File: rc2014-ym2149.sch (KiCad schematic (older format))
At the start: 23 parts, among them J1 JACK_TRS_6PINS, P1 CONN_01X35, P2 CONN_02X08, P3 AY-3-8190/YM2149F, P4 IO Out, U1 74HCT138, U3 74HCT00, U4 74HCT74

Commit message: Messing about with address decoding
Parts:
- added J? (x2): CONN_02X08, symbol CONN_02X08
- added J?: CONN_02X03, symbol CONN_02X03
- added U? (x2): 74HCT00, symbol 74HCT00
- added U?: 74LS138, symbol 74LS138
- P2: value CONN_02X08 -> CONN_02X09; symbol CONN_02X08 -> CONN_02X09
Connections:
- net labels added: /AY_CS, /E2, E3, REG
- wire segments 166 -> 248
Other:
- moved on the sheet: U1, U3A, U3B

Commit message: More work on PCB
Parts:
- removed J?: CONN_02X08, symbol CONN_02X08
- removed P2: CONN_02X09, Pin_Headers:Pin_Header_Straight_2x08_Pitch2.54mm, symbol CONN_02X09
- removed U? (x2): 74HCT00, symbol 74HCT00
- removed U?: 74LS138, symbol 74LS138
- added C7: C, Capacitors_THT:C_Disc_D3.8mm_W2.6mm_P2.50mm, symbol C
- added J2, J3: CONN_02X02, Pin_Headers:Pin_Header_Straight_2x02_Pitch2.54mm, symbol CONN_02X02
- added U2: 74HCT138, Housings_DIP:DIP-16_W7.62mm_Socket, symbol 74LS138
- added unit 3 of U3
- added unit 4 of U3
- J4: renamed from J?; footprint (none) -> Pin_Headers:Pin_Header_Straight_2x03_Pitch2.54mm
- J5: renamed from J?; footprint (none) -> Pin_Headers:Pin_Header_Straight_2x08_Pitch2.54mm
- P1: value CONN_01X35 -> RC2014 BUS; footprint Pin_Headers:Pin_Header_Angled_1x35_Pitch2.54mm -> Pin_Headers:Pin_Header_Angled_1x39_Pitch2.54mm; symbol CONN_01X35 -> CONN_01X39
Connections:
- net labels added: CS
- net labels removed: /AY_CS, /E2, E3
- wire segments 248 -> 210
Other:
- moved on the sheet: C4, C6, J5

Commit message: WIP
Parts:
- J1: value JACK_TRS_6PINS -> AUDIO OUT
- JP1: renamed from J2; value CONN_02X02 -> USE A4 FOR ENABLE; symbol CONN_02X02 -> Jumper_Dual
- JP2: renamed from J3; value CONN_02X02 -> ENABLE SELECTOR; symbol CONN_02X02 -> Jumper_Dual
- JP4: renamed from J5; value CONN_02X08 -> BASE ADDRESS
- JP5: renamed from JP1; value Jumper_Dual -> CLOCK DIVIDE 1/2 or 1/4
- renumbered C4 to C1, C5 to C2, C6 to C3, C7 to C4, C1 to C5, C2 to C6, C3 to C7, P4 to J2, J4 to JP3, JP3 to JP6, U2 to U1, U1 to U2, P3 to U5
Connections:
- wire segments 210 -> 207
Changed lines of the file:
@@
 $EndComp
 $Comp
-L DIL40 P3
+L DIL40 U5
 U 1 1 58979138
 P 6600 3100
-F 0 "P3" H 6600 4150 50  0000 C CNN
+F 0 "U5" H 6600 4150 50  0000 C CNN
 F 1 "AY-3-8190/YM2149F" V 6600 3100 50  0000 C CNN
 F 2 "Housings_DIP:DIP-40_W15.24mm_Socket" H 6600 3100 50  0001 C CNN
@@
 $EndComp
 $Comp
-L 74LS138 U1
+L 74LS138 U2
 U 1 1 589793B1
 P 3450 3200
-F 0 "U1" H 3550 3700 50  0000 C CNN
+F 0 "U2" H 3550 3700 50  0000 C CNN
 F 1 "74HCT138" H 3600 2651 50  0000 C CNN
 F 2 "Housings_DIP:DIP-16_W7.62mm_Socket" H 3450 3200 50  0001 C CNN
@@
 P 10150 1000
 F 0 "J1" H 10150 1400 50  0000 C CNN
-F 1 "JACK_TRS_6PINS" H 10100 700 50  0000 C CNN
+F 1 "AUDIO OUT" H 10100 700 50  0000 C CNN
 F 2 "rc2014:cliff_fcr1295_socket" H 10250 850 50  0001 C CNN
 F 3 "" H 10250 850 50  0000 C CNN
@@
 $EndComp
 $Comp
-L C C1
+L C C5
 U 1 1 58B2B931
 P 7200 2000
-F 0 "C1" H 7225 2100 50  0000 L CNN
+F 0 "C5" H 7225 2100 50  0000 L CNN
 F 1 "0.1uF" H 7225 1900 50  0000 L CNN
 F 2 "Capacitors_THT:C_Disc_D3.8mm_W2.6mm_P2.50mm" H 7238 1850 50  0001 C CNN
@@
 	1    0    0    -1
 $EndComp
-Text Label 2700 2950 0    60   ~ 0
+Text Label 2650 2950 0    60   ~ 0
 /WR
-Text Label 2700 3050 0    60   ~ 0
+Text Label 2650 3050 0    60   ~ 0
 /RD
-Text Label 2700 3550 0    60   ~ 0
+Text Label 2650 3550 0    60   ~ 0
 /IORQ
 $Comp
-L Jumper JP3
+L Jumper JP6
 U 1 1 58BC56E2
 P 8650 3550
-F 0 "JP3" H 8650 3700 50  0000 C CNN
+F 0 "JP6" H 8650 3700 50  0000 C CNN
 F 1 "YM 1/2 CLK" H 8650 3470 50  0000 C CNN
 F 2 "Pin_Headers:Pin_Header_Straight_1x02_Pitch2.54mm" H 8650 3550 50  0001 C CNN
@@
 	6000 4150 6100 4050
 $Comp
-L CONN_02X09 P4
+L CONN_02X09 J2
 U 1 1 58BC7A79
 P 10450 2700
-F 0 "P4" H 10450 3200 50  0000 C CNN
+F 0 "J2" H 10450 3200 50  0000 C CNN
 F 1 "IO Out" V 10450 2700 50  0000 C CNN
 F 2 "Pin_Headers:Pin_Header_Straight_2x09_Pitch2.54mm" H 10450 1500 50  0001 C CNN
@@
 	7350 4100 7450 4200
 $Comp
-L CP C2
+L CP C6
 U 1 1 58BDC9B3
 P 9000 800
-F 0 "C2" H 9025 900 50  0000 L CNN
+F 0 "C6" H 9025 900 50  0000 L CNN
 F 1 "470uF" H 9025 700 50  0000 L CNN
 F 2 "Capacitors_THT:CP_Radial_D5.0mm_P2.50mm" H 9038 650 50  0001 C CNN
@@
 $EndComp
 $Comp
-L CP C3
+L CP C7
 U 1 1 58BDCA34
 P 9000 1000
-F 0 "C3" H 9025 1100 50  0000 L CNN
+F 0 "C7" H 9025 1100 50  0000 L CNN
 F 1 "470uF" H 9025 900 50  0000 L CNN
 F 2 "Capacitors_THT:CP_Radial_D5.0mm_P2.50mm" H 9038 850 50  0001 C CNN
@@
 D7
 $Comp
-L C C4
+L C C1
 U 1 1 58C9A12D
 P 2550 6400
-F 0 "C4" H 2575 6500 50  0000 L CNN
+F 0 "C1" H 2575 6500 50  0000 L CNN
 F 1 "C" H 2575 6300 50  0000 L CNN
 F 2 "Capacitors_THT:C_Disc_D3.8mm_W2.6mm_P2.50mm" H 2588 6250 50  0001 C CNN
@@
 $EndComp
 $Comp
-L C C5
+L C C2
 U 1 1 58C9A196
 P 2900 6400
-F 0 "C5" H 2925 6500 50  0000 L CNN
+F 0 "C2" H 2925 6500 50  0000 L CNN
 F 1 "C" H 2925 6300 50  0000 L CNN
 F 2 "Capacitors_THT:C_Disc_D3.8mm_W2.6mm_P2.50mm" H 2938 6250 50  0001 C CNN
@@
 $EndComp
 $Comp
-L C C6
+L C C3
 U 1 1 58C9A1DD
 P 3250 6400
-F 0 "C6" H 3275 6500 50  0000 L CNN
+F 0 "C3" H 3275 6500 50  0000 L CNN
 F 1 "C" H 3275 6300 50  0000 L CNN
 F 2 "Capacitors_THT:C_Disc_D3.8mm_W2.6mm_P2.50mm" H 3288 6250 50  0001 C CNN
@@
 BC1
 $Comp
-L Jumper_Dual JP1
+L Jumper_Dual JP5
 U 1 1 58D043AC
 P 7450 5350
-F 0 "JP1" H 7500 5250 50  0000 L CNN
-F 1 "Jumper_Dual" H 7450 5450 50  0000 C BNN
+F 0 "JP5" H 7500 5250 50  0000 L CNN
+F 1 "CLOCK DIVIDE 1/2 or 1/4" H 7450 5450 50  0000 C BNN
 F 2 "Pin_Headers:Pin_Header_Straight_1x03_Pitch2.54mm" H 7450 5350 50  0001 C CNN
 F 3 "" H 7450 5350 50  0001 C CNN
@@
 Text Label 2700 2850 0    60   ~ 0
 REG
-Text Label 2750 3450 0    60   ~ 0
+Text Label 2650 3450 0    60   ~ 0
 A1
 Wire Wire Line
@@
 	1100 4100 1350 4100
 Wire Wire Line
-	2900 2950 2700 2950
-Wire Wire Line
-	2900 3050 2700 3050
-Wire Wire Line
-	2900 3550 2700 3550
+	2850 2950 2650 2950
+Wire Wire Line
+	2850 3050 2650 3050
 Connection ~ 7200 2150
 Wire Wire Line
@@
 	7700 5100 7700 5350
 Wire Wire Line
-	2500 3350 2850 3350
-Wire Wire Line
-	2850 3450 2700 3450
+	2250 3350 2850 3350
 Wire Wire Line
 	1100 1800 1350 1800
@@
 Wire Wire Line
 	2600 2850 2850 2850
-Text Label 1850 3350 0    60   ~ 0
+Text Label 1800 3200 0    60   ~ 0
 A15
 $Comp
-L CONN_02X03 J4
+L CONN_02X03 JP3
 U 1 1 58DAC18B
 P 2300 2700
-F 0 "J4" H 2300 2900 50  0000 C CNN
+F 0 "JP3" H 2300 2900 50  0000 C CNN
 F 1 "CONN_02X03" H 2300 2500 50  0000 C CNN
 F 2 "Pin_Headers:Pin_Header_Straight_2x03_Pitch2.54mm" H 2300 1500 50  0001 C CNN
@@
 Wire Wire Line
 	2050 2800 1850 2800
-Text Label 1900 2700 0    60   ~ 0
+Text Label 1850 2700 0    60   ~ 0
 A3
-Text Label 1900 2800 0    60   ~ 0
+Text Label 1850 2800 0    60   ~ 0
 A2
-Text Label 1900 2600 0    60   ~ 0
+Text Label 1850 2600 0    60   ~ 0
 A14
 $Comp
-L CONN_02X08 J5
+L CONN_02X08 JP4
 U 1 1 58DAD194
 P 3550 1150
-F 0 "J5" H 3550 1600 50  0000 C CNN
-F 1 "CONN_02X08" V 3550 1150 50  0000 C CNN
+F 0 "JP4" H 3550 1600 50  0000 C CNN
+F 1 "BASE ADDRESS" V 3550 1150 50  0000 C CNN
 F 2 "Pin_Headers:Pin_Header_Straight_2x08_Pitch2.54mm" H 3550 -50 50  0001 C CNN
 F 3 "" H 3550 -50 50  0001 C CNN
@@
 Connection ~ 3950 1500
 $Comp
-L 74LS138 U2
+L 74LS138 U1
 U 1 1 58DAFD76
 P 2550 1150
-F 0 "U2" H 2650 1650 50  0000 C CNN
+F 0 "U1" H 2650 1650 50  0000 C CNN
 F 1 "74HCT138" H 2700 601 50  0000 C CNN
 F 2 "Housings_DIP:DIP-16_W7.62mm_Socket" H 2550 1150 50  0001 C CNN
@@
 Wire Wire Line
 	1950 1000 1700 1000
-Wire Wire Line
-	1550 1300 1950 1300
 Wire Wire Line
 	1950 1400 1700 1400
@@
 A7
 $Comp
-L CONN_02X02 J2
+L Jumper_Dual JP1
 U 1 1 58DB01E6
-P 1300 1250
-F 0 "J2" H 1300 1400 50  0000 C CNN
-F 1 "CONN_02X02" H 1300 1100 50  0000 C CNN
-F 2 "Pin_Headers:Pin_Header_Straight_2x02_Pitch2.54mm" H 1300 50  50  0001 C CNN
-F 3 "" H 1300 50  50  0001 C CNN
-	1    1300 1250
-	1    0    0    -1
-$EndComp
-Wire Wire Line
-	1550 1200 1600 1200
-Wire Wire Line
-	1600 1200 1600 1300
-Connection ~ 1600 1300
+P 1100 1100
+F 0 "JP1" H 1100 1250 50  0000 C CNN
+F 1 "USE A4 FOR ENABLE" H 1150 800 50  0000 C CNN
+F 2 "Pin_Headers:Pin_Header_Straight_2x02_Pitch2.54mm" H 1100 -100 50  0001 C CNN
+F 3 "" H 1100 -100 50  0001 C CNN
+	1    1100 1100
+	1    0    0    -1
+$EndComp
 Wire Wire Line
 	1700 1400 1700 1600
@@
 	1    0    0    -1
 $EndComp
-Wire Wire Line
-	1050 1200 850  1200
-Wire Wire Line
-	1050 1300 850  1300
-Text Label 900  1300 0    60   ~ 0
+Text Label 1400 1100 0    60   ~ 0
 A4
 $Comp
 L VCC #PWR024
 U 1 1 58DB09C6
-P 850 1200
-F 0 "#PWR024" H 850 1050 50  0001 C CNN
-F 1 "VCC" H 850 1350 50  0000 C CNN
-F 2 "" H 850 1200 50  0001 C CNN
-F 3 "" H 850 1200 50  0001 C CNN
-	1    850  1200
-	1    0    0    -1
+P 850 1100
+F 0 "#PWR024" H 850 950 50  0001 C CNN
+F 1 "VCC" H 850 1250 50  0000 C CNN
+F 2 "" H 850 1100 50  0001 C CNN
+F 3 "" H 850 1100 50  0001 C CNN
+	1    850  1100
+	0    -1   -1   0
 $EndComp
 Connection ~ 1700 1500
@@
 CS
 $Comp
-L CONN_02X02 J3
+L Jumper_Dual JP2
 U 1 1 58DB0BB0
-P 2250 3400
-F 0 "J3" H 2250 3550 50  0000 C CNN
-F 1 "CONN_02X02" H 2250 3250 50  0000 C CNN
-F 2 "Pin_Headers:Pin_Header_Straight_2x02_Pitch2.54mm" H 2250 2200 50  0001 C CNN
-F 3 "" H 2250 2200 50  0001 C CNN
-	1    2250 3400
-	1    0    0    -1
-$EndComp
-Wire Wire Line
-	2000 3350 1850 3350
-Wire Wire Line
-	2000 3450 1850 3450
-Wire Wire Line
-	2500 3450 2550 3450
-Wire Wire Line
-	2550 3450 2550 3350
-Connection ~ 2550 3350
-Text Label 1850 3450 0    60   ~ 0
+P 2250 3200
+F 0 "JP2" H 2250 3350 50  0000 C CNN
+F 1 "ENABLE SELECTOR" H 2250 2850 50  0000 C CNN
+F 2 "Pin_Headers:Pin_Header_Straight_2x02_Pitch2.54mm" H 2250 2000 50  0001 C CNN
+F 3 "" H 2250 2000 50  0001 C CNN
+	1    2250 3200
+	1    0    0    -1
+$EndComp
+Text Label 2550 3200 0    60   ~ 0
 CS
 $Comp
@@
 $EndComp
 $Comp
-L C C7
+L C C4
 U 1 1 58DB1AE2
 P 3600 6400
-F 0 "C7" H 3625 6500 50  0000 L CNN
+F 0 "C4" H 3625 6500 50  0000 L CNN
 F 1 "C" H 3625 6300 50  0000 L CNN
 F 2 "Capacitors_THT:C_Disc_D3.8mm_W2.6mm_P2.50mm" H 3638 6250 50  0001 C CNN
@@
 	1    0    0    -1
 $EndComp
+Wire Wire Line
+	2850 3450 2650 3450
+Wire Wire Line
+	2850 3550 2650 3550
+Wire Wire Line
+	1350 1100 1550 1100
+Wire Wire Line
+	1100 1300 1950 1300
+Wire Wire Line
+	1100 1300 1100 1200
+Wire Wire Line
+	2000 3200 1800 3200
+Wire Wire Line
+	2500 3200 2750 3200
+Wire Wire Line
+	2250 3350 2250 3300
 $EndSCHEMATC

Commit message: Fix all ERC errors
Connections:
- no-connect marks 0 -> 25
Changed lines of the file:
@@
 	1100 3400 1650 3400
 Wire Wire Line
-	1100 3500 1350 3500
+	1100 3500 1450 3500
 Wire Wire Line
 	1100 3700 1350 3700
@@
 Wire Wire Line
 	2250 3350 2250 3300
+$Comp
+L PWR_FLAG #FLG028
+U 1 1 58E0E873
+P 1550 3400
+F 0 "#FLG028" H 1550 3475 50  0001 C CNN
+F 1 "PWR_FLAG" H 1550 3550 50  0000 C CNN
+F 2 "" H 1550 3400 50  0001 C CNN
+F 3 "" H 1550 3400 50  0001 C CNN
+	1    1550 3400
+	1    0    0    -1
+$EndComp
+Connection ~ 1550 3400
+$Comp
+L PWR_FLAG #FLG029
+U 1 1 58E0EDBF
+P 1450 3500
+F 0 "#FLG029" H 1450 3575 50  0001 C CNN
+F 1 "PWR_FLAG" H 1450 3650 50  0000 C CNN
+F 2 "" H 1450 3500 50  0001 C CNN
+F 3 "" H 1450 3500 50  0001 C CNN
+	1    1450 3500
+	1    0    0    -1
+$EndComp
+Connection ~ 1350 3500
+NoConn ~ 1100 5200
+NoConn ~ 1100 5300
+NoConn ~ 1100 5400
+NoConn ~ 1100 5500
+NoConn ~ 1100 5600
+NoConn ~ 1350 3900
+NoConn ~ 1350 4000
+NoConn ~ 1350 3600
+NoConn ~ 1350 3300
+NoConn ~ 1350 2500
+NoConn ~ 1350 2400
+NoConn ~ 1350 2300
+NoConn ~ 1350 2200
+NoConn ~ 1350 2100
+NoConn ~ 1350 2000
+NoConn ~ 6250 2250
+NoConn ~ 6250 2550
+NoConn ~ 6950 2250
+NoConn ~ 4050 2850
+NoConn ~ 4050 2950
+NoConn ~ 4050 3050
+NoConn ~ 4050 3450
+NoConn ~ 4050 3550
+NoConn ~ 5650 1150
+NoConn ~ 5650 1850
 $EndSCHEMATC

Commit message: Add ground fill and create gerbers
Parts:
- JP1, JP2: footprint Pin_Headers:Pin_Header_Straight_2x02_Pitch2.54mm -> Pin_Headers:Pin_Header_Straight_1x03_Pitch2.54mm
- P1: footprint Pin_Headers:Pin_Header_Angled_1x39_Pitch2.54mm -> rc2014:Pin_Header_Straight_1x39_Pitch2.54mm_NoSilk
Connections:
- wire segments 207 -> 209
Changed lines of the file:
@@
 F 0 "P1" H 900 5750 50  0000 C CNN
 F 1 "RC2014 BUS" V 1000 3700 50  0000 C CNN
-F 2 "Pin_Headers:Pin_Header_Angled_1x39_Pitch2.54mm" H 900 3700 50  0001 C CNN
+F 2 "rc2014:Pin_Header_Straight_1x39_Pitch2.54mm_NoSilk" H 900 3700 50  0001 C CNN
 F 3 "" H 900 3700 50  0000 C CNN
 	1    900  3700
-	-1   0    0    1
+	-1   0    0    -1
 $EndComp
 $Comp
@@
 	4850 5100 5100 5100
 Wire Wire Line
-	8050 3950 8050 5650
-Wire Wire Line
 	4600 5300 5100 5300
 Wire Wire Line
@@
 Wire Wire Line
 	6300 6650 6900 6650
-Wire Wire Line
-	6300 5100 7700 5100
-Wire Wire Line
-	6900 6650 6900 5350
 Wire Bus Line
 	6000 2750 6000 4200
@@
 Connection ~ 9600 800
 Wire Wire Line
-	8050 5650 7450 5650
-Wire Wire Line
 	7450 5650 7450 5450
 Wire Wire Line
-	6900 5350 7200 5350
-Wire Wire Line
-	7700 5100 7700 5350
-Wire Wire Line
 	2250 3350 2850 3350
 Wire Wire Line
@@
 Wire Wire Line
 	2600 2850 2850 2850
-Text Label 1800 3200 0    60   ~ 0
+Text Label 2600 3200 0    60   ~ 0
 A15
 $Comp
@@
 F 0 "JP1" H 1100 1250 50  0000 C CNN
 F 1 "USE A4 FOR ENABLE" H 1150 800 50  0000 C CNN
-F 2 "Pin_Headers:Pin_Header_Straight_2x02_Pitch2.54mm" H 1100 -100 50  0001 C CNN
+F 2 "Pin_Headers:Pin_Header_Straight_1x03_Pitch2.54mm" H 1100 -100 50  0001 C CNN
 F 3 "" H 1100 -100 50  0001 C CNN
 	1    1100 1100
@@
 F 0 "JP2" H 2250 3350 50  0000 C CNN
 F 1 "ENABLE SELECTOR" H 2250 2850 50  0000 C CNN
-F 2 "Pin_Headers:Pin_Header_Straight_2x02_Pitch2.54mm" H 2250 2000 50  0001 C CNN
+F 2 "Pin_Headers:Pin_Header_Straight_1x03_Pitch2.54mm" H 2250 2000 50  0001 C CNN
 F 3 "" H 2250 2000 50  0001 C CNN
 	1    2250 3200
 	1    0    0    -1
 $EndComp
-Text Label 2550 3200 0    60   ~ 0
+Text Label 1800 3200 0    60   ~ 0
 CS
 $Comp
@@
 NoConn ~ 5650 1150
 NoConn ~ 5650 1850
+Wire Wire Line
+	8050 5650 7450 5650
+Wire Wire Line
+	8050 3950 8050 5650
+Wire Wire Line
+	6900 6650 6900 5850
+Wire Wire Line
+	6900 5850 7700 5850
+Wire Wire Line
+	7700 5850 7700 5350
+Wire Wire Line
+	6300 5100 6850 5100
+Wire Wire Line
+	6850 5100 6850 5350
+Wire Wire Line
+	6850 5350 7200 5350
 $EndSCHEMATC

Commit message: Update readme, remove non project stuff
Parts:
- JP1: MPN (none) -> CONN 1x03
- R1: Base number (none) -> 470R Through Hole Resistor, 470 ohm, 250 V, Axial Leaded, 2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; MPN (none) -> MF25 470R; Supplier URL (none) -> http://uk.farnell.com/multicomp/mf25-470r/resistor-470r-0-2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
- R4: Description (none) -> 1K Through Hole Resistor, 1 kohm, 250 V, Axial Leaded, 250 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; MPN (none) -> MF25 1K; Supplier URL (none) -> http://uk.farnell.com/multicomp/mf25-1k/resistor-1k-0-25w-1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
- R6: Description (none) -> MF25 1K6 Through Hole Resistor, 1.6 kohm, 250 V, Axial Lead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; MPN (none) -> MF25 1K6; Supplier URL (none) -> http://uk.farnell.com/multicomp/mf25-1k6/resistor-0-25w-1-1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
- U1, U2: Base number (none) -> 74HCT138; MPN (none) -> CD74HCT138E; Supplier URL (none) -> http://uk.farnell.com/texas-instruments/cd74hct138e/74hct-c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
- U3: MPN (none) -> SN74HCT00N; Supplier URL (none) -> http://uk.farnell.com/texas-instruments/sn74hct00n/quad-2-i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
- U4: Base number (none) -> 74HCT74; MPN (none) -> SN74HCT74N; Supplier URL (none) -> http://uk.farnell.com/texas-instruments/sn74hct74n/ic-flip-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
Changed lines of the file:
@@
 F 2 "Housings_DIP:DIP-16_W7.62mm_Socket" H 3450 3200 50  0001 C CNN
 F 3 "" H 3450 3200 50  0000 C CNN
+F 4 "CD74HCT138E" H 3450 3200 60  0001 C CNN "MPN"
+F 5 "74HCT138" H 3450 3200 60  0001 C CNN "Base number"
+F 6 "http://uk.farnell.com/texas-instruments/cd74hct138e/74hct-cmos-74hct138-dip16-5-5v/dp/1105976" H 3450 3200 60  0001 C CNN "Supplier URL"
 	1    3450 3200
 	1    0    0    -1
@@
 F 2 "Housings_DIP:DIP-14_W7.62mm_Socket" H 5700 5300 50  0001 C CNN
 F 3 "" H 5700 5300 50  0000 C CNN
+F 4 "SN74HCT74N" H 5700 5300 60  0001 C CNN "MPN"
+F 5 "74HCT74" H 5700 5300 60  0001 C CNN "Base number"
+F 6 "http://uk.farnell.com/texas-instruments/sn74hct74n/ic-flip-flop-2-circuits/dp/1470823" H 5700 5300 60  0001 C CNN "Supplier URL"
 	1    5700 5300
 	1    0    0    -1
@@
 F 2 "Resistors_THT:R_Axial_DIN0207_L6.3mm_D2.5mm_P7.62mm_Horizontal" H 8300 600 50  0001 C CNN
 F 3 "" H 8300 600 50  0000 C CNN
+F 4 "MF25 1K" H 8300 600 60  0001 C CNN "MPN"
+F 5 "1K  Through Hole Resistor, 1 kohm, 250 V, Axial Leaded, 250 mW, ± 1%" H 8300 600 60  0001 C CNN "Description"
+F 6 "http://uk.farnell.com/multicomp/mf25-1k/resistor-1k-0-25w-1/dp/9341102" H 8300 600 60  0001 C CNN "Supplier URL"
 	1    8300 600
 	0    1    1    0
@@
 F 2 "Resistors_THT:R_Axial_DIN0207_L6.3mm_D2.5mm_P7.62mm_Horizontal" H 8300 1000 50  0001 C CNN
 F 3 "" H 8300 1000 50  0000 C CNN
+F 4 "MF25 1K6" H 8300 1000 60  0001 C CNN "MPN"
+F 5 "MF25 1K6  Through Hole Resistor, 1.6 kohm, 250 V, Axial Leaded, 250 mW, ± 1%" H 8300 1000 60  0001 C CNN "Description"
+F 6 "http://uk.farnell.com/multicomp/mf25-1k6/resistor-0-25w-1-1k6/dp/9341382" H 8300 1000 60  0001 C CNN "Supplier URL"
 	1    8300 1000
 	0    1    1    0
@@
 F 2 "Resistors_THT:R_Axial_DIN0207_L6.3mm_D2.5mm_P7.62mm_Horizontal" H 7300 1350 50  0001 C CNN
 F 3 "" H 7300 1350 50  0000 C CNN
+F 4 "MF25 470R" H 7300 1350 60  0001 C CNN "MPN"
+F 5 "470R  Through Hole Resistor, 470 ohm, 250 V, Axial Leaded, 250 mW, ± 1%" H 7300 1350 60  0001 C CNN "Base number"
+F 6 "http://uk.farnell.com/multicomp/mf25-470r/resistor-470r-0-25w-1/dp/9341943" H 7300 1350 60  0001 C CNN "Supplier URL"
 	1    7300 1350
 	1    0    0    -1
@@
 F 2 "Housings_DIP:DIP-16_W7.62mm_Socket" H 2550 1150 50  0001 C CNN
 F 3 "" H 2550 1150 50  0000 C CNN
+F 4 "CD74HCT138E" H 2550 1150 60  0001 C CNN "MPN"
+F 5 "74HCT138" H 2550 1150 60  0001 C CNN "Base number"
+F 6 "http://uk.farnell.com/texas-instruments/cd74hct138e/74hct-cmos-74hct138-dip16-5-5v/dp/1105976" H 2550 1150 60  0001 C CNN "Supplier URL"
 	1    2550 1150
 	1    0    0    -1
@@
 F 2 "Pin_Headers:Pin_Header_Straight_1x03_Pitch2.54mm" H 1100 -100 50  0001 C CNN
 F 3 "" H 1100 -100 50  0001 C CNN
+F 4 "CONN 1x03" H 1100 1100 60  0001 C CNN "MPN"
 	1    1100 1100
 	1    0    0    -1
@@
 F 2 "Housings_DIP:DIP-14_W7.62mm_Socket" H 5050 1150 50  0001 C CNN
 F 3 "" H 5050 1150 50  0001 C CNN
+F 4 "SN74HCT00N" H 5050 1150 60  0001 C CNN "MPN"
+F 5 "http://uk.farnell.com/texas-instruments/sn74hct00n/quad-2-input-nand-74hct00-dip14/dp/9591745" H 5050 1150 60  0001 C CNN "Supplier URL"
 	3    5050 1150
 	1    0    0    -1

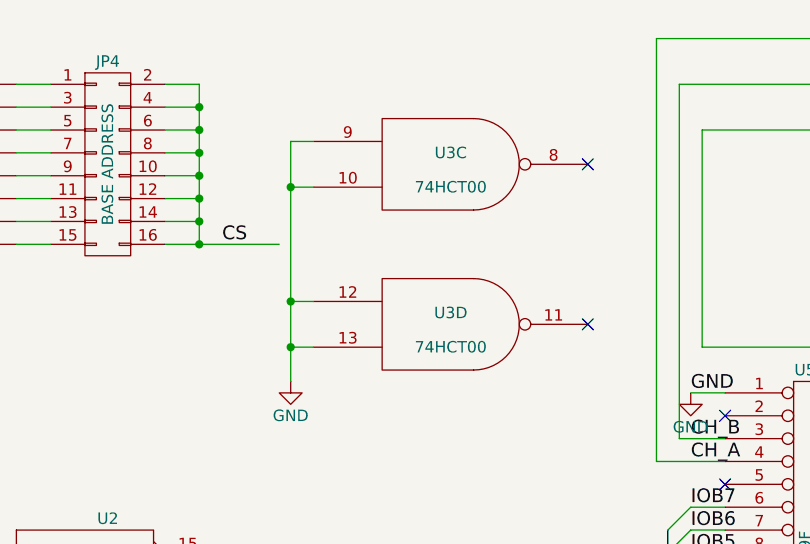
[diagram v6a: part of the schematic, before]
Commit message: Use NAND to invert output from first 74HCT138
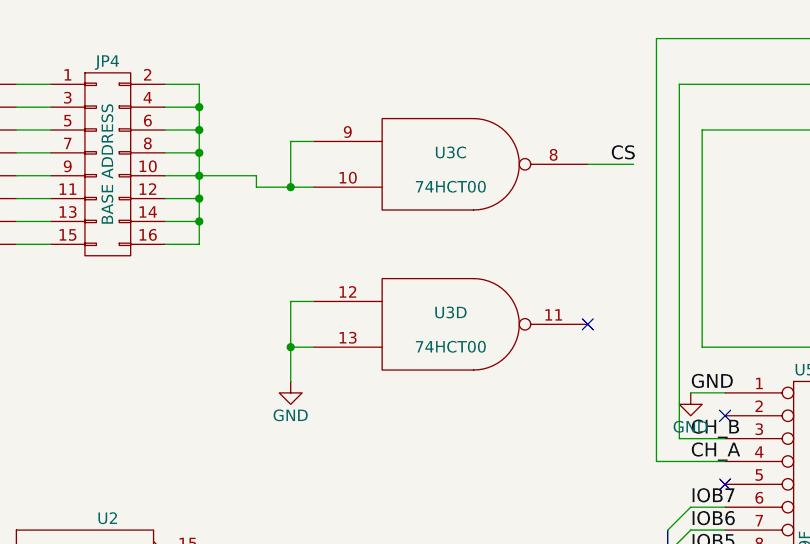
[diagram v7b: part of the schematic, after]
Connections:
- wire segments 209 -> 212
- no-connect marks 25 -> 24
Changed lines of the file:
@@
 Sheet 1 1
 Title "RC2014 YM2149 / AY-3-8910 sound card"
-Date "2017-02-05"
-Rev "1"
+Date "2017-04-29"
+Rev "2"
 Comp ""
 Comment1 ""
@@
 	3950 800  3950 1500
 Wire Wire Line
-	3800 1500 4300 1500
-Wire Wire Line
 	3800 900  3950 900
 Connection ~ 3950 900
@@
 Connection ~ 3950 1100
 Wire Wire Line
-	3800 1200 3950 1200
+	3800 1200 4200 1200
 Connection ~ 3950 1200
 Wire Wire Line
@@
 	3800 1400 3950 1400
 Connection ~ 3950 1400
-Connection ~ 3950 1500
 $Comp
 L 74LS138 U1
@@
 $EndComp
 Connection ~ 1700 1500
-Text Label 4050 1500 0    60   ~ 0
+Text Label 5750 1150 0    60   ~ 0
 CS
 $Comp
@@
 	4450 1050 4350 1050
 Wire Wire Line
-	4350 1050 4350 2100
-Wire Wire Line
-	4450 1250 4350 1250
+	4200 1250 4450 1250
 Connection ~ 4350 1250
 Wire Wire Line
 	4450 1750 4350 1750
-Connection ~ 4350 1750
 Wire Wire Line
 	4450 1950 4350 1950
@@
 NoConn ~ 4050 3450
 NoConn ~ 4050 3550
-NoConn ~ 5650 1150
 NoConn ~ 5650 1850
 Wire Wire Line
@@
 Wire Wire Line
 	6850 5350 7200 5350
+Wire Wire Line
+	4350 1750 4350 2100
+Wire Wire Line
+	5650 1150 5850 1150
+Wire Wire Line
+	4200 1200 4200 1250
+Wire Wire Line
+	4350 1050 4350 1250
+Wire Wire Line
+	3950 1500 3800 1500
 $EndSCHEMATC
